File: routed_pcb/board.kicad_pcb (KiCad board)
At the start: 2 copper layers, 100 x 100 mm, 31 parts

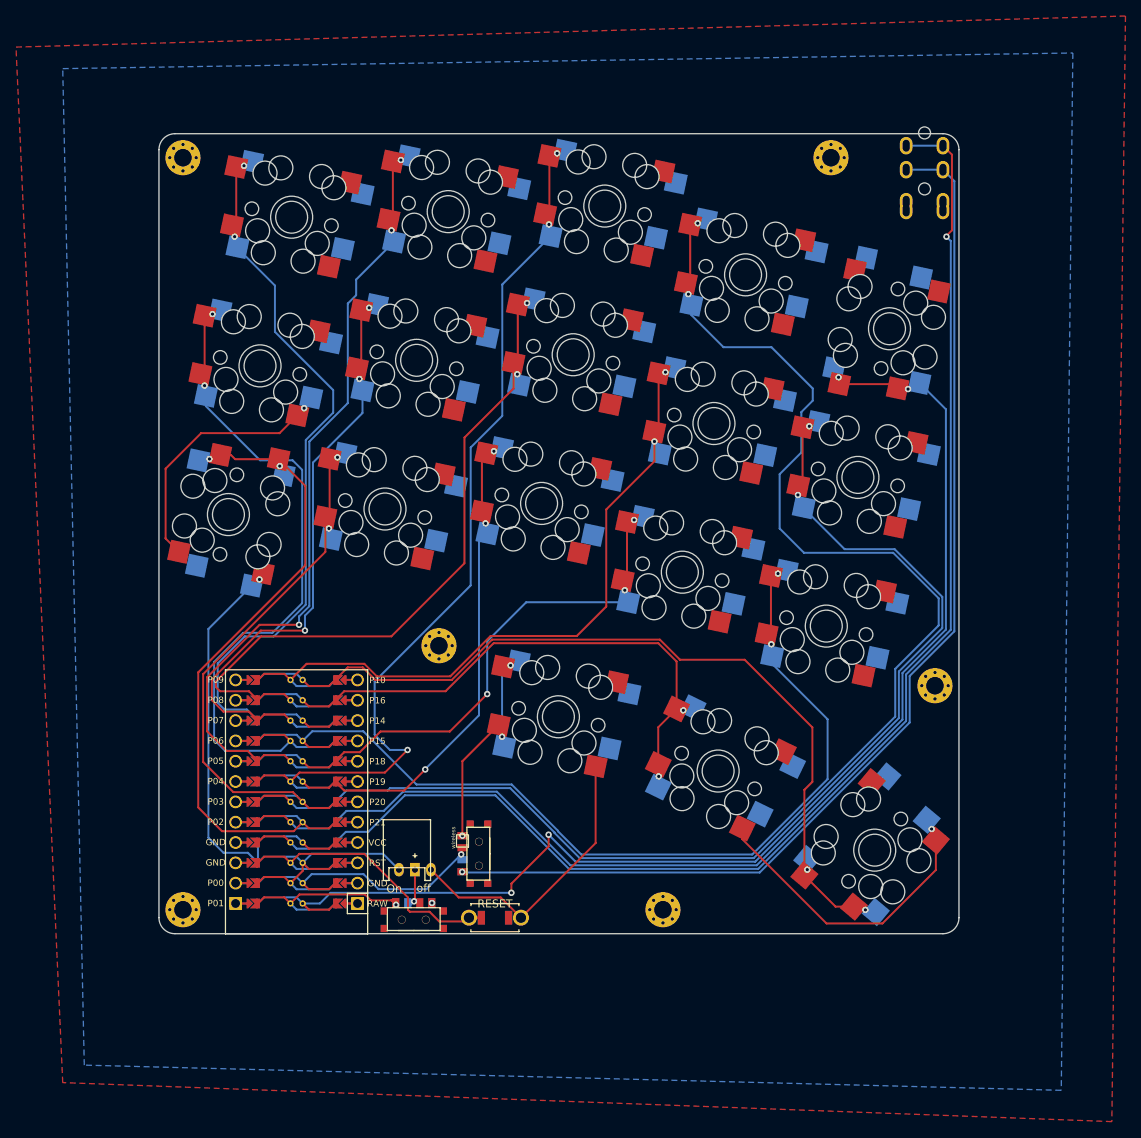
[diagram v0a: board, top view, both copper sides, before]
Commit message: updated images, moved output pcb to routed (not actually routed yet)
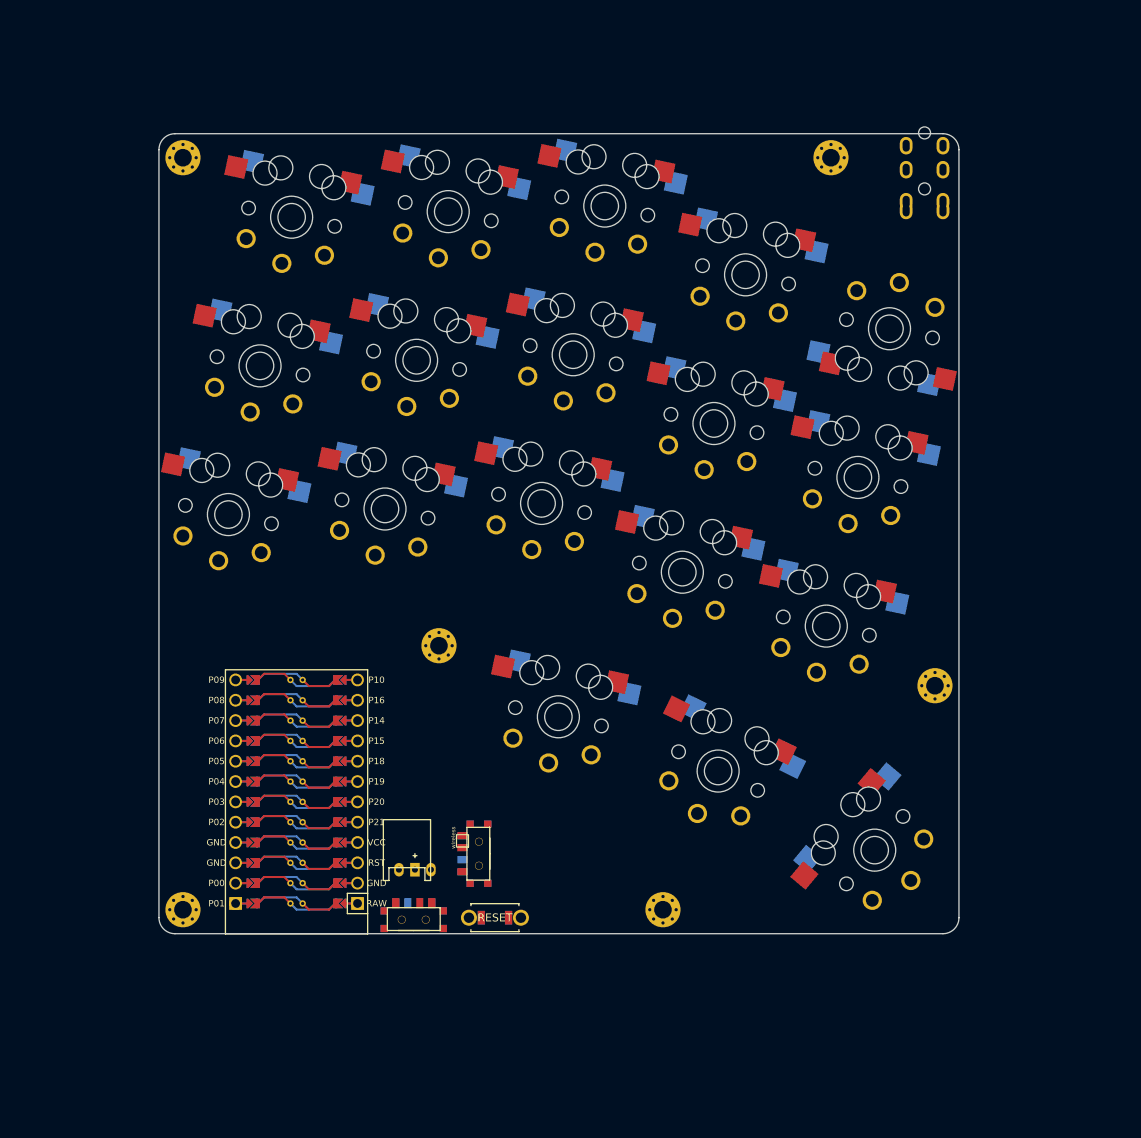
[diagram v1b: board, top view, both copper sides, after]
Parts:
- B1, B2, JST1, MCU1, SW1, SW10, SW11, SW12, SW13, SW14, SW15, SW16, SW17, SW18, SW2, SW3, SW4, SW5, SW6, SW7, SW8, SW9, T1, T2: value ~ -> (none)
- turned SW15 to 168 degrees
- turned SW1 to -12 degrees
- turned B2 to 0 degrees
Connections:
- net /Bplus renamed Bplus
- net /GND renamed GND
- net /P0 renamed P0
- net /RAW renamed RAW
- net /RST renamed RST
- net /VCC renamed VCC
- net /matrix_index_bottom renamed matrix_index_bottom
- net /matrix_index_home renamed matrix_index_home
- net /matrix_index_top renamed matrix_index_top
- net /matrix_inner_bottom renamed matrix_inner_bottom
- net /matrix_inner_home renamed matrix_inner_home
- net /matrix_inner_top renamed matrix_inner_top
- net /matrix_middle_bottom renamed matrix_middle_bottom
- net /matrix_middle_home renamed matrix_middle_home
- net /matrix_middle_top renamed matrix_middle_top
- net /matrix_pinky_bottom renamed matrix_pinky_bottom
- net /matrix_pinky_home renamed matrix_pinky_home
- net /matrix_pinky_top renamed matrix_pinky_top
- net /matrix_ring_bottom renamed matrix_ring_bottom
- net /matrix_ring_home renamed matrix_ring_home
- net /matrix_ring_top renamed matrix_ring_top
- net /thumb_inner renamed thumb_inner
- net /thumb_reachy renamed thumb_reachy
- net /thumb_tucky renamed thumb_tucky
- net /trrs_data renamed trrs_data
- T1 pad 3: unconnected-(T1-C-Pad3) -> (no net)
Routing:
- net matrix_index_top: track 174.5 -> 0.00 mm, vias 2 -> 0
- net GND: track 169.6 -> 0.00 mm, vias 3 -> 0
- net VCC: track 165.2 -> 0.00 mm, vias 1 -> 0
- net matrix_inner_top: track 142.4 -> 0.00 mm, vias 2 -> 0
- net matrix_inner_home: track 140.7 -> 0.00 mm, vias 4 -> 0
- net trrs_data: track 140.4 -> 0.00 mm, vias 1 -> 0
- net matrix_inner_bottom: track 107.5 -> 0.00 mm, vias 2 -> 0
- net matrix_middle_top: track 105.4 -> 0.00 mm, vias 3 -> 0
- net thumb_reachy: track 99.5 -> 0.00 mm, vias 2 -> 0
- net matrix_ring_top: track 94.5 -> 0.00 mm, vias 3 -> 0
- net matrix_pinky_top: track 88.8 -> 0.00 mm, vias 2 -> 0
- net matrix_middle_home: track 84.2 -> 0.00 mm, vias 2 -> 0
- net matrix_index_home: track 80.5 -> 0.00 mm, vias 2 -> 0
- net matrix_pinky_home: track 80.5 -> 0.00 mm, vias 2 -> 0
- net matrix_pinky_bottom: track 78.0 -> 0.00 mm, vias 2 -> 0
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- removed copper zone on B.Cu, net GND
- removed copper zone on F.Cu, net GND
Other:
- net class Default added: clearance 0.2, trace_width 0.25, via_dia 0.8, via_drill 0.4
- board text removed: "On"
- board text removed: "off"
